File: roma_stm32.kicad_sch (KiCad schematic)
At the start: 16 parts, among them J1 CAN, J2 Power, J3 Debug_Port, J4 GPIO, J5 I2C, J6 SPI, J7 UART, SW1 SW_RST, U2 STM32L432KBUx

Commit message: WIP: Prepare for JLC
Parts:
- removed C6: 10uF, Capacitor_SMD:C_0603_1608Metric, symbol Device:C
- added R5: 1K8, Resistor_SMD:R_0603_1608Metric, symbol Device:R
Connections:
- net +3V3: now also R5.1
- net at SW1.2, U2.4 (NRST): now also R5.2
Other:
- moved on the sheet: SW1

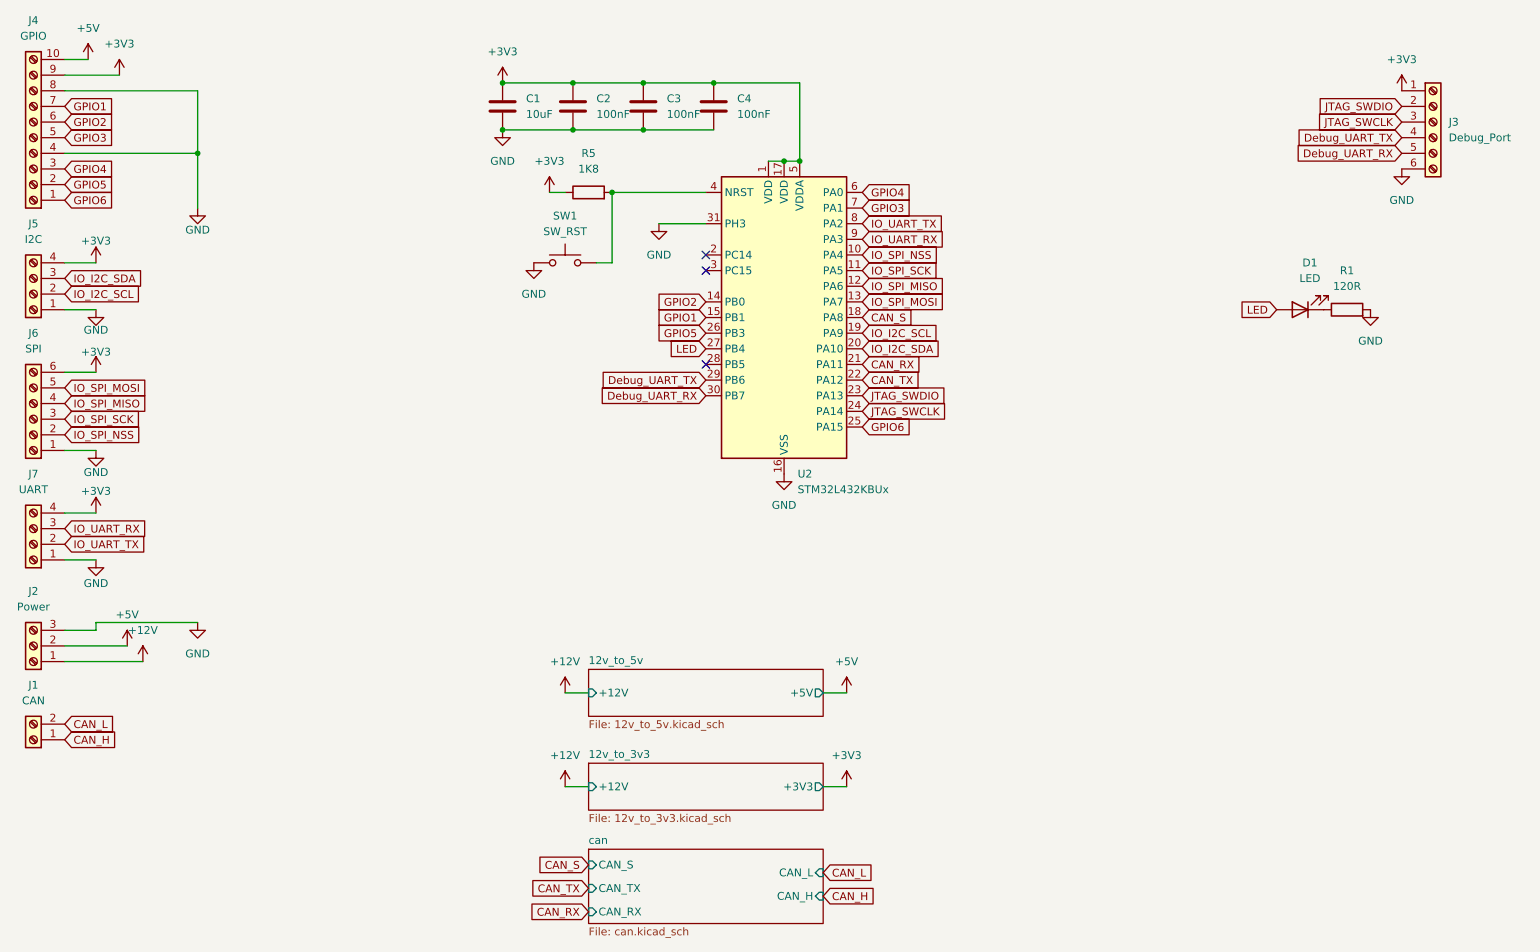
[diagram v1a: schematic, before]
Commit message: Replace power regulators; Pick all JLC components
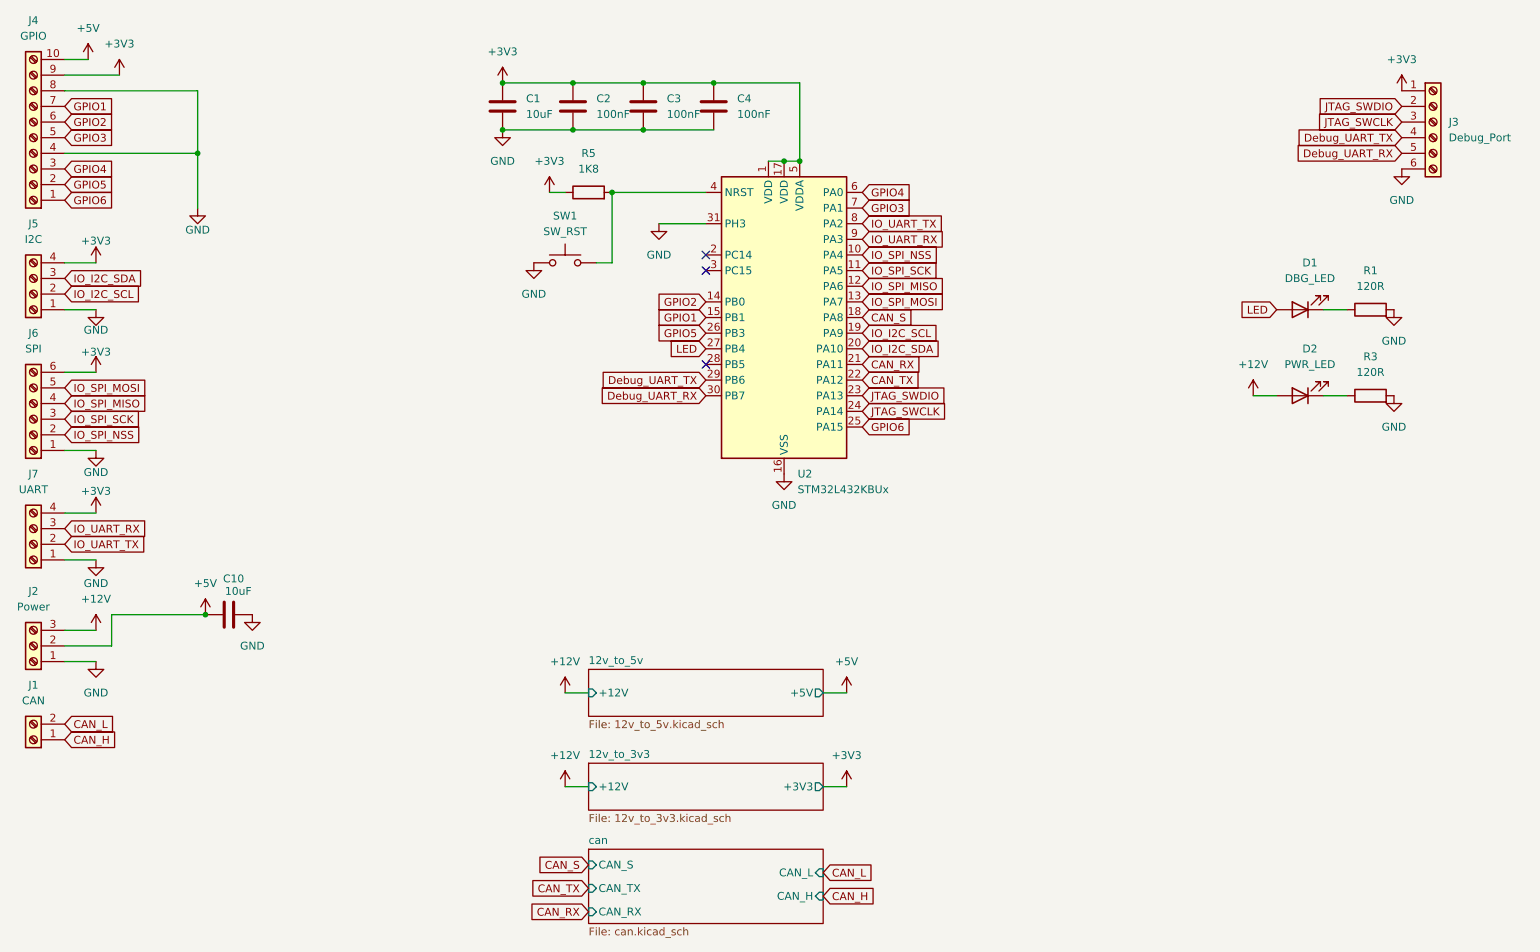
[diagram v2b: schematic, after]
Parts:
- added C10: 10uF, Capacitor_SMD:C_0805_2012Metric, symbol Device:C
- added D2: PWR_LED, LED_SMD:LED_0805_2012Metric, symbol Device:LED
- added R3: 120R, Resistor_SMD:R_0805_2012Metric, symbol Device:R
- C1: footprint Capacitor_SMD:C_0603_1608Metric -> Capacitor_SMD:C_0805_2012Metric
- D1: value LED -> DBG_LED; footprint LED_SMD:LED_0402_1005Metric -> LED_SMD:LED_0805_2012Metric
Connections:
- net +12V: now also J2.3 (Pin_3), D2.2 (A); no longer J2.1 (Pin_1)
- net +5V: now also C10.1
- net GND: now also J2.1 (Pin_1), C10.2, R3.2; no longer J2.3 (Pin_3)
- new net: D2.1 (K), R3.1
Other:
- moved on the sheet: R1
